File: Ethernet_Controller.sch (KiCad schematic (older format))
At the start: 41 parts, among them J1 SS-60000-009, T1 749020010A, U1 RTL8111H, Y1 ABM8G-25.000MHZ-18-D2Y-T

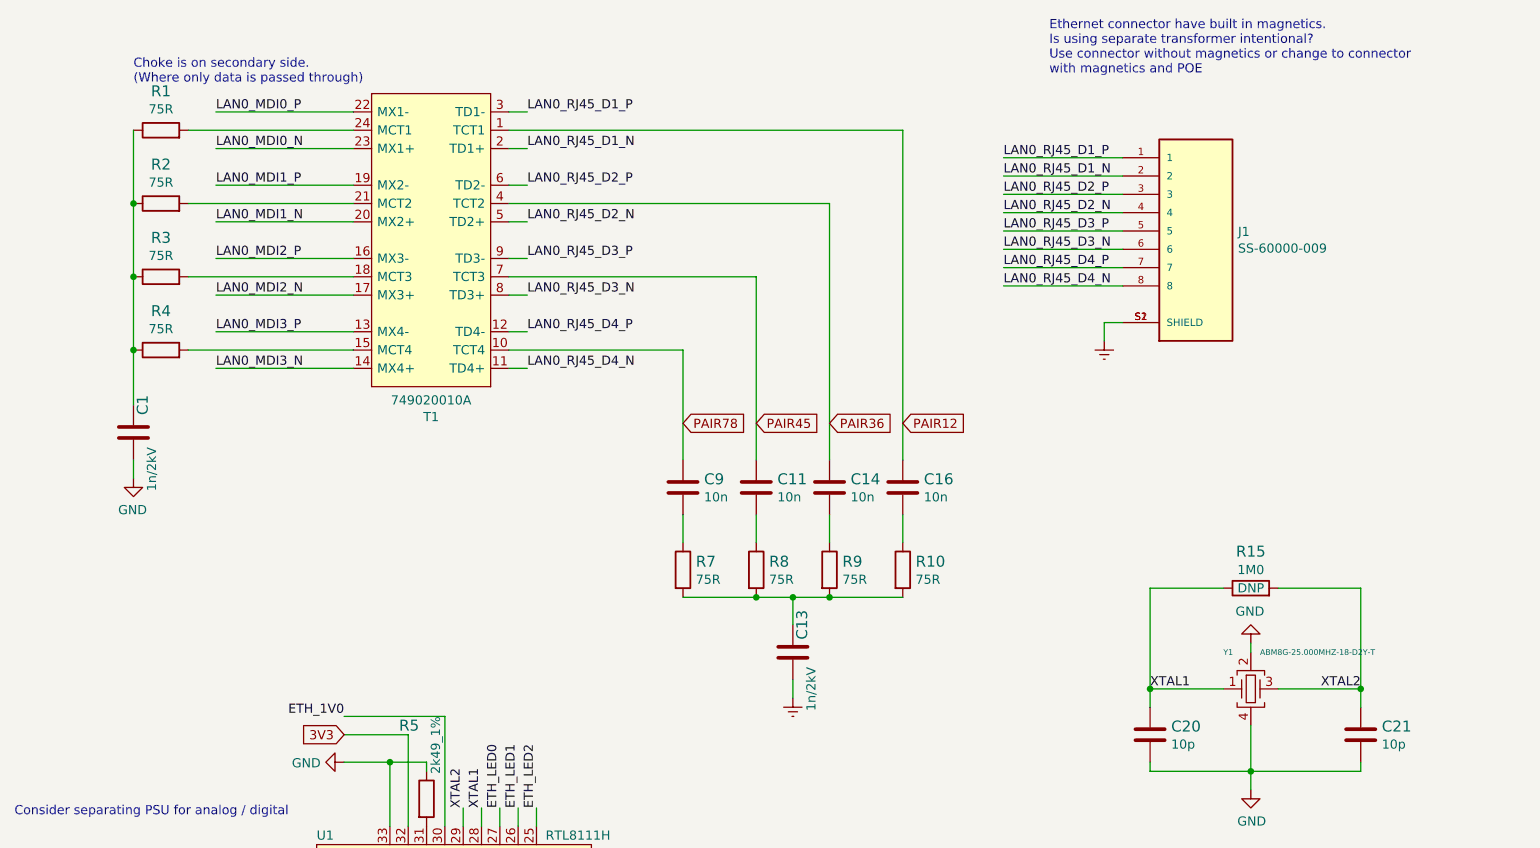
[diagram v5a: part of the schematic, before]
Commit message: finished rebuilding ethernet connector
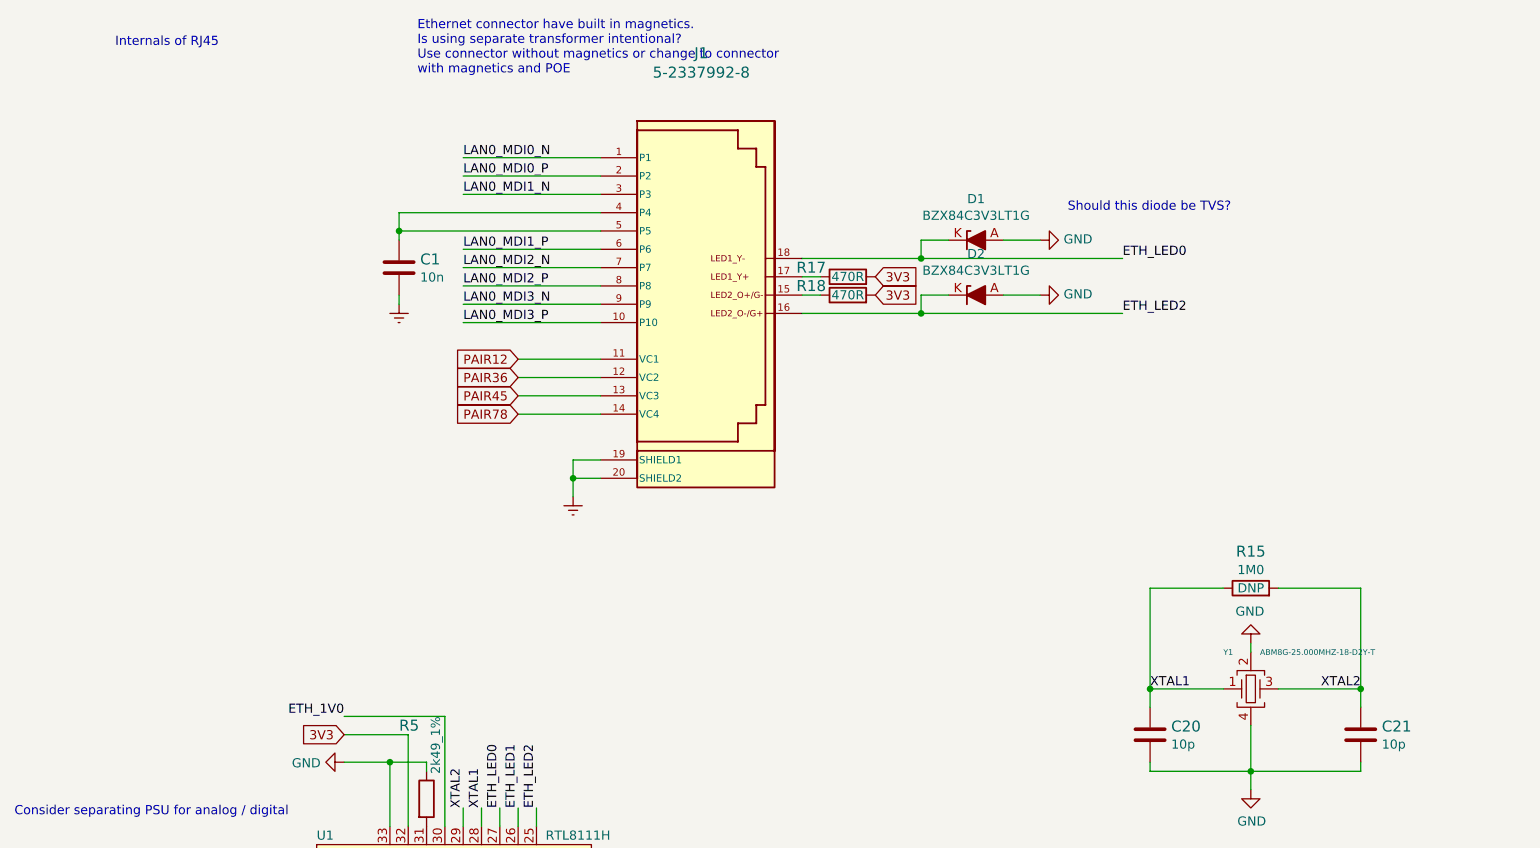
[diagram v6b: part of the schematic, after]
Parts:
- removed C1, C13: C_1n_1210_2kV, sa800u-baseboard-hw-footprints:1210-cap, symbol sa800u-baseboard-hw:C_1n_1210_2kV
- removed C11, C14, C16, C9: C_10n_0402, sa800u-baseboard-hw-footprints:0402-cap, symbol sa800u-baseboard-hw:C_10n_0402
- removed J1: SS-60000-009, antmicro-footprints:BEL_SS-60000-009, symbol antmicroModularConnectorsJacks:SS-60000-009
- removed R1, R10, R2, R3, R4, R7, R8, R9: R_75R_0402, sa800u-baseboard-hw-footprints:0402-res, symbol sa800u-baseboard-hw:R_75R_0402
- removed T1: 749020010A, sa800u-baseboard-hw-footprints:749020010A, symbol sa800u-baseboard-hw:749020010A
- added C1: C_10n_0402, antmicro-footprints:0402-cap, symbol antmicroCapacitors0402:C_10n_0402
- added D1, D2: BZX84C3V3LT1G, antmicro-footprints:SOT-23-3, symbol antmicroDiodesZenerSingle:BZX84C3V3LT1G
- added J1: 5-2337992-8, antmicro-footprints:5-2337992-8, symbol antmicroModularConnectorsJacksWithMagnetics:5-2337992-8
- added R17, R18: R_470R_0402, sa800u-baseboard-hw-footprints:0402-res, symbol sa800u-baseboard-hw:R_470R_0402
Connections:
- net 3V3: now also R17.2, R18.2
- net ETH_LED0: now also D1.K, J1.18
- net ETH_LED2: now also D2.K, J1.16
- net Earth: now also C1.2, J1.19 (SHIELD1), J1.20 (SHIELD2)
- net GND: now also D1.A, D2.A
- net LAN0_MDI0_N: now also J1.1 (P1)
- net LAN0_MDI0_P: now also J1.2 (P2)
- net LAN0_MDI1_N: now also J1.3 (P3)
- net LAN0_MDI1_P: now also J1.6 (P6)
- net LAN0_MDI2_N: now also J1.7 (P7)
- net LAN0_MDI2_P: now also J1.8 (P8)
- net LAN0_MDI3_N: now also J1.9 (P9)
- net LAN0_MDI3_P: now also J1.10 (P10)
- net PAIR12: now also J1.11 (VC1)
- net PAIR36: now also J1.12 (VC2)
- net PAIR45: now also J1.13 (VC3)
- net PAIR78: now also J1.14 (VC4)
- new net: J1.15, R18.1
- new net: J1.17, R17.1
- new net: C1.1, J1.4 (P4), J1.5 (P5)
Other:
- note added: "Internals of RJ45"
- note added: "Should this diode be TVS?"
- note removed: "Choke is on secondary side.\n(Where only data is passed through)"

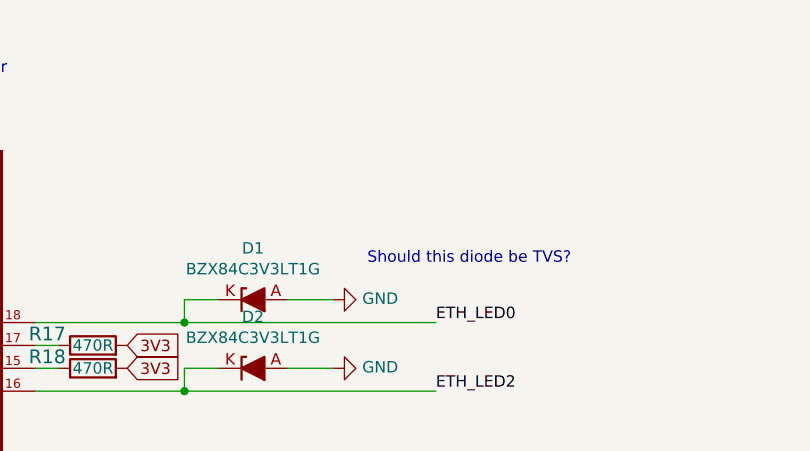
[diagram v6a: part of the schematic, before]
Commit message: added reference to chineese replacement of RJ45
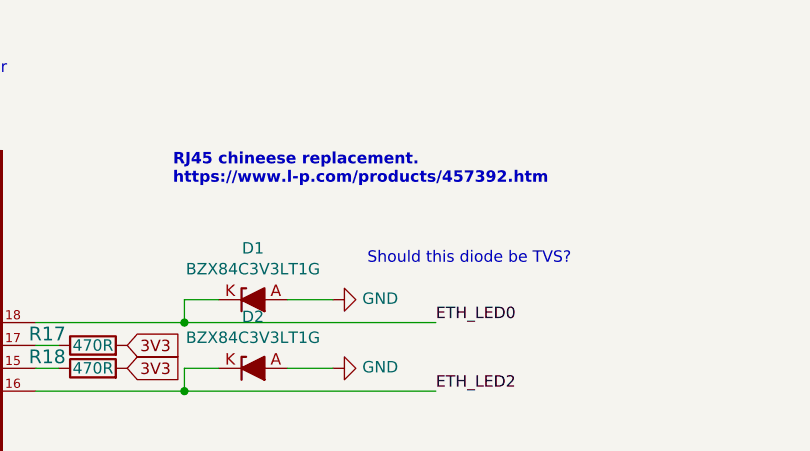
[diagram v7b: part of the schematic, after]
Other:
- note added: "RJ45 chineese replacement. \nhttps://www.l-p.com/products/457392.htm"
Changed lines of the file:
@@
 Text Notes 6700 1650 0    50   ~ 0
 Should this diode be TVS?
+Text Notes 5850 1300 0    50   ~ 10
+RJ45 chineese replacement. \nhttps://www.l-p.com/products/457392.htm
 $EndSCHEMATC
